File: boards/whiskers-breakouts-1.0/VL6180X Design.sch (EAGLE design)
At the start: 25 parts, among them J2 6-PIN_2MM-V, Q3 BSS138, Q4 BSS138, U1 VL6180X, U2 TLV74128PDBVR, U3 VL6180X, U4 VL6180X, U5 MIC5225-3.3YM5-TR

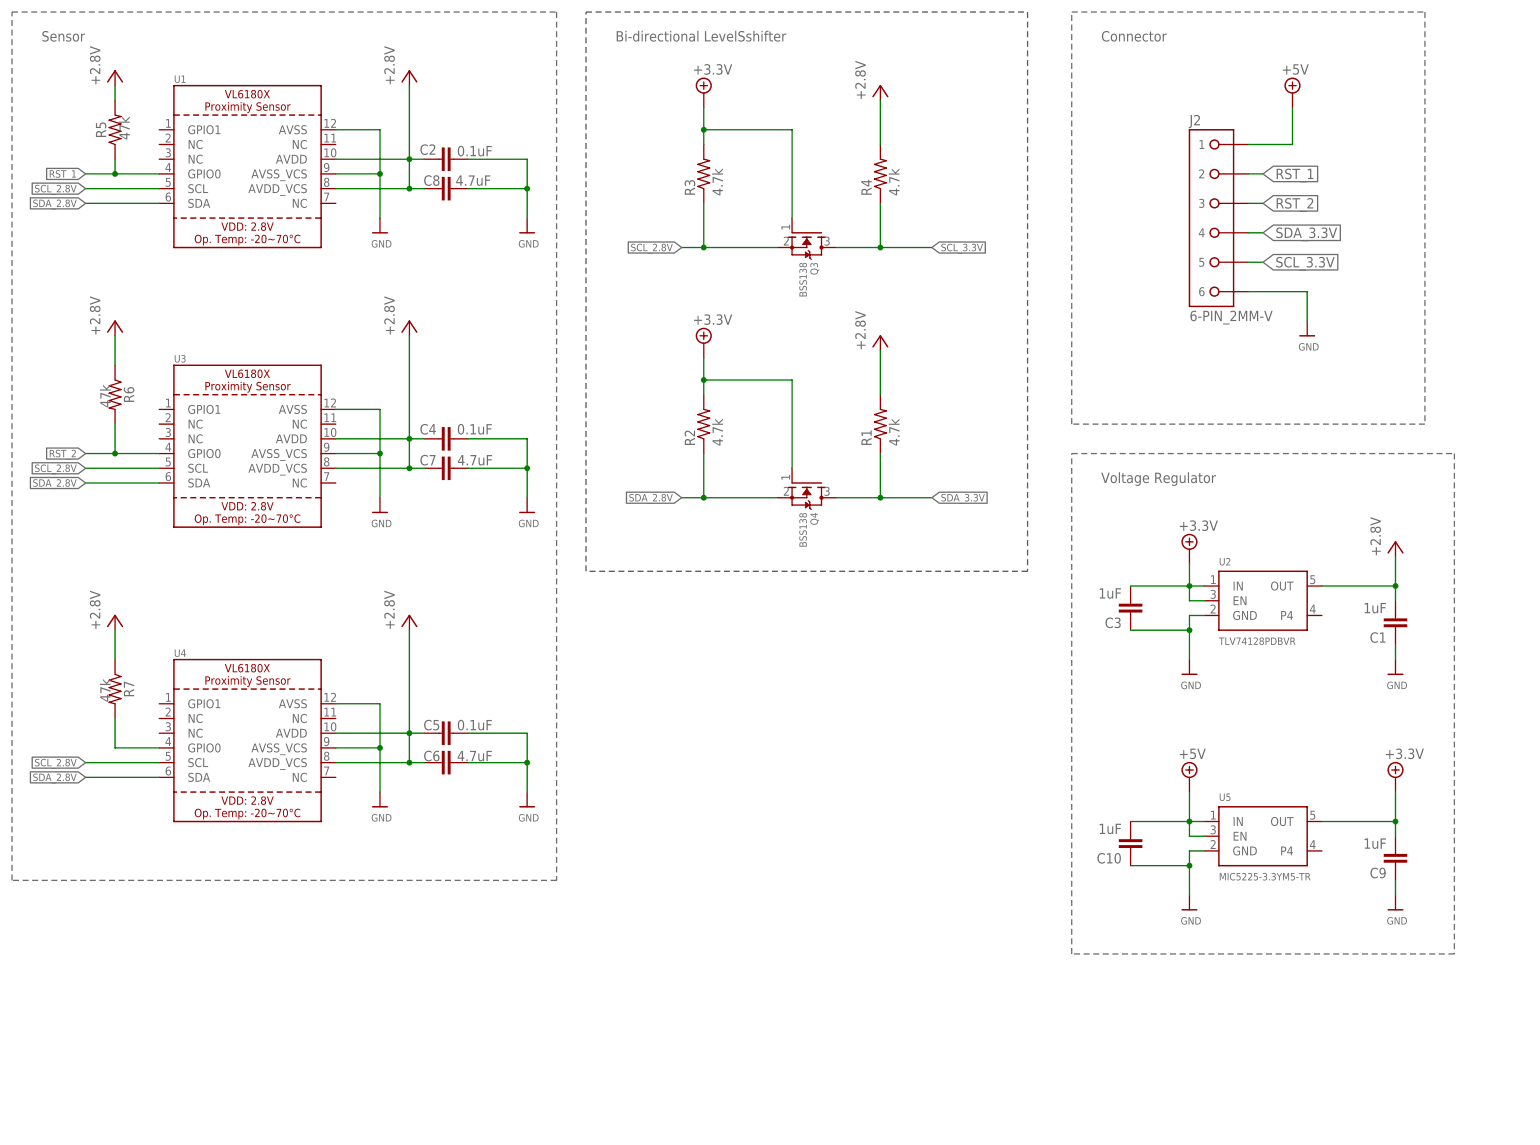
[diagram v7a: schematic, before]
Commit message: Corrected Schematic
This should complete the corrected schematic. Big Changes Include a BiDirectional Level Shifter IC instead of our old bi directional level shifter and two voltage regulators to ensure compatibility with control board.
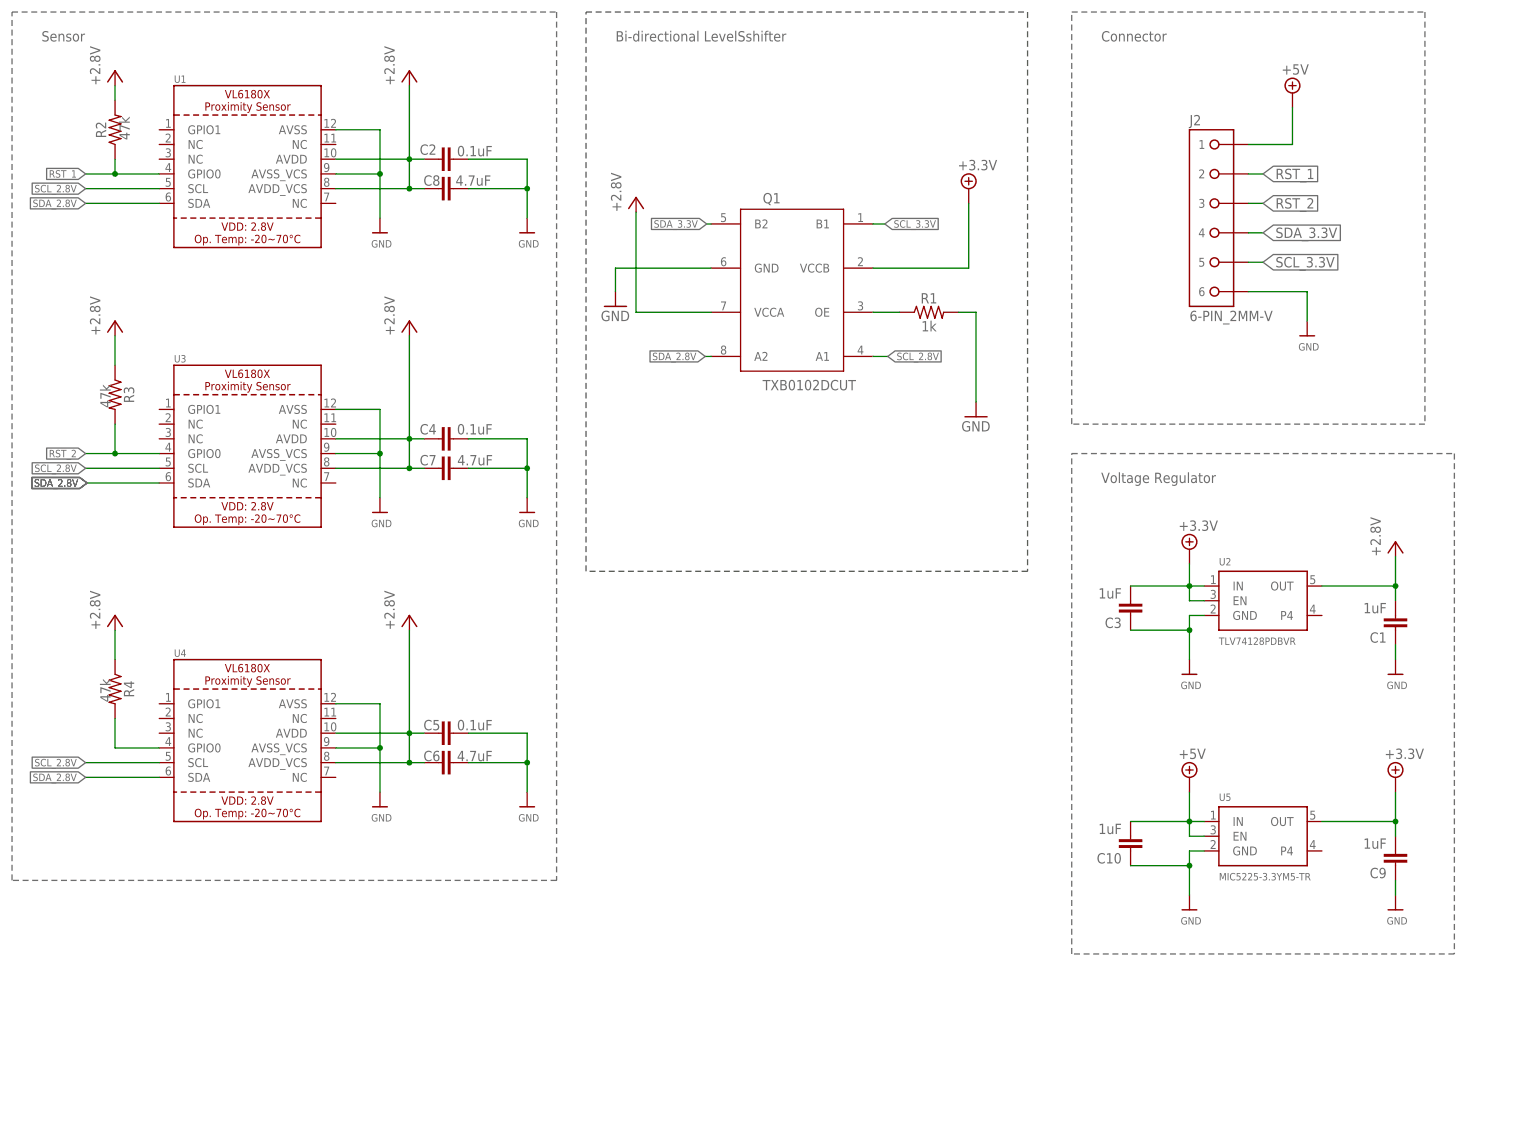
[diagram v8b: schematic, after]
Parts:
- removed Q3, Q4: BSS138, microbuilder:MOSFET-NWIDE
- removed R5, R6, R7: 47k, SparkFun-Resistors:0.05OHM-0603-1/5W-1%
- added Q1: TXB0102DCUT, RoboJackets-ICs:TXB0102DCUT
- R1: value 4.7k -> 1k; device RoboJackets-Resistors:R0603W -> SparkFun-Resistors:0.05OHM-0603-1/5W-1%
- R2, R3, R4: value 4.7k -> 47k; device RoboJackets-Resistors:R0603W -> SparkFun-Resistors:0.05OHM-0603-1/5W-1%
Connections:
- new net N$1: Q1.OE, R1.1
- net +3.3V: now also Q1.VCCB; no longer Q3.G, Q4.G, R2.PIN2, R3.PIN2
- net GND: now also Q1.GND, R1.2
- net RST_1: now also R2.1; no longer R5.1
- net RST_2: now also R3.2; no longer R6.2
- net RST_3: now also R4.2; no longer R7.2
- net SCL_2.8V: now also Q1.A1; no longer Q3.S, R3.PIN1
- net SCL_3.3V: now also Q1.B1; no longer Q3.D, R4.PIN1
- net SDA_2.8V: now also Q1.A2; no longer Q4.S, R2.PIN1
- net SDA_3.3V: now also Q1.B2; no longer Q4.D, R1.PIN1
- net VCC: now also Q1.VCCA, R2.2, R3.1, R4.1; no longer R1.PIN2, R4.PIN2, R5.2, R6.1, R7.1
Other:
- moved on the sheet: R1, R2, R3, R4
